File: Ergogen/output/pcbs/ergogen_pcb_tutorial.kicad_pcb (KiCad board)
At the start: 2 copper layers, 241.1 x 108.8 mm, 75 parts

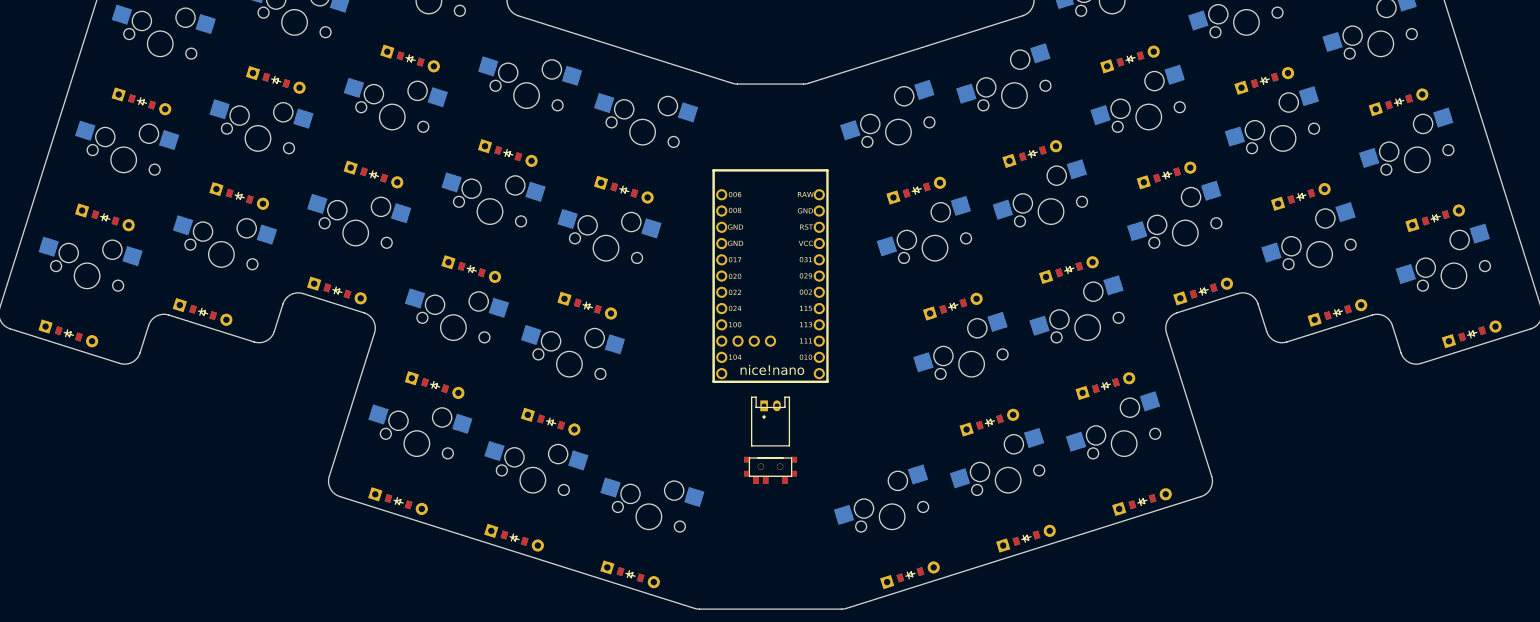
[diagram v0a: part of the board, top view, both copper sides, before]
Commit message: new changes, updated ergogen footprints for slider switch and nice nano (to have thirteen pins)
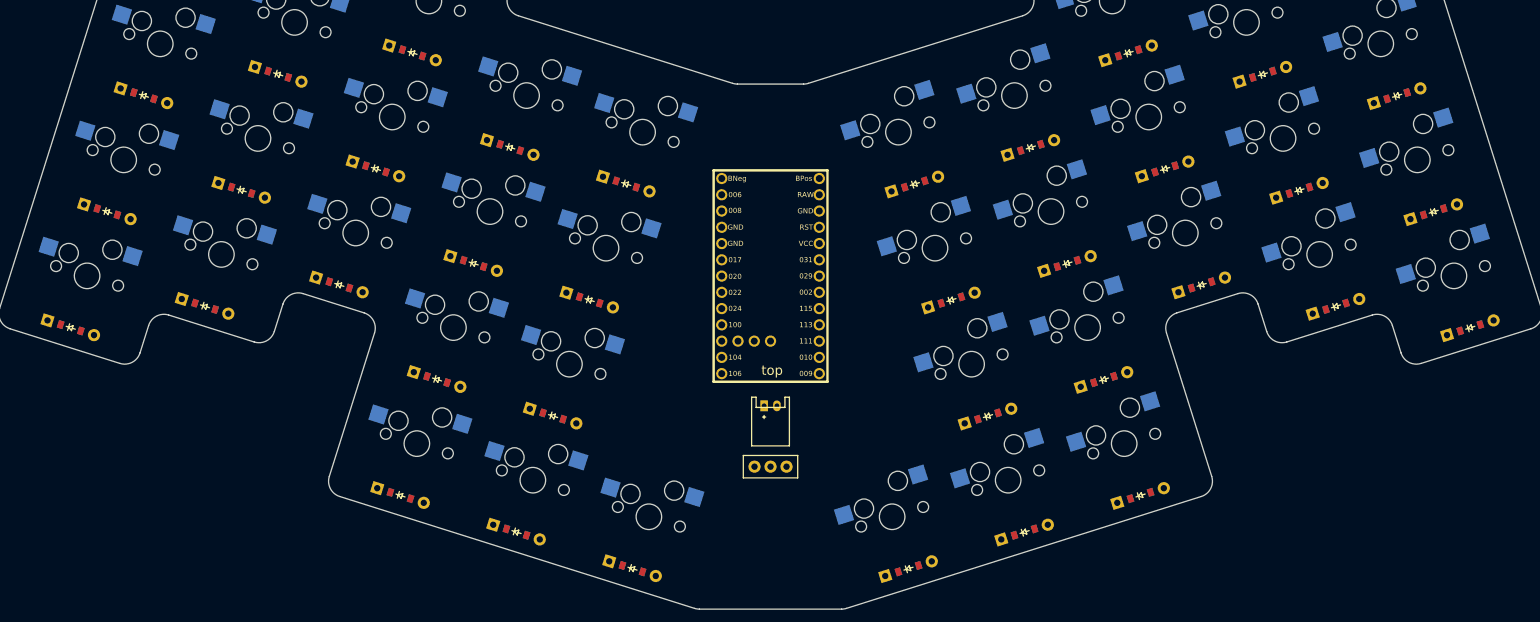
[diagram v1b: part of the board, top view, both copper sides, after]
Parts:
- T1: value (none) -> 1test slide switch; footprint E73:SPDT_C128955 -> 1test_slide_switch
- moved D1 1.00 mm to (62.7, 133.5)
- moved D10 1.00 mm to (120.0, 141.6)
- moved D13 1.00 mm to (138.1, 147.3)
- moved D16 1.00 mm to (114.3, 159.7)
- moved D17 1.00 mm to (132.4, 165.5)
- moved D18 1.00 mm to (150.5, 171.2)
- moved D19 1.00 mm to (281.3, 133.5)
- moved D28 1.00 mm to (224.1, 141.6)
- moved D31 1.00 mm to (206.0, 147.3)
- moved D34 1.00 mm to (229.8, 159.7)
- moved D35 1.00 mm to (211.7, 165.5)
- moved D36 1.00 mm to (193.6, 171.2)
- moved D11 1.00 mm to (125.7, 123.5)
- moved D12 1.00 mm to (131.4, 105.4)
- moved D15 1.00 mm to (149.5, 111.1)
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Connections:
- MCU1 pad 10: P011 -> P100
- MCU1 pad 11: P104 -> P011
- MCU1 pad 12: P106 -> P104
- MCU1 pad 13: P009 -> P106
- MCU1 pad 14: P010 -> P009
- MCU1 pad 15: P111 -> P010
- MCU1 pad 16: P113 -> P111
- MCU1 pad 17: P115 -> P113
- MCU1 pad 18: P002 -> P115
- MCU1 pad 19: P029 -> P002
- MCU1 pad 2: P008 -> P006
- MCU1 pad 20: P031 -> P029
- MCU1 pad 21: VCC -> P031
- MCU1 pad 22: RST -> VCC
- MCU1 pad 23: GND -> RST
- MCU1 pad 24: RAW -> GND
- MCU1 pad 3: GND -> P008
- MCU1 pad 5: P017 -> GND
- MCU1 pad 6: P020 -> P017
- MCU1 pad 7: P022 -> P020
- MCU1 pad 8: P024 -> P022
- MCU1 pad 9: P100 -> P024
- T1 pad 1: RAW -> BPos
